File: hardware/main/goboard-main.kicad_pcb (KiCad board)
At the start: 2 copper layers, 304.7 x 114.2 mm, 190 parts, among them J1 USB_C_Receptacle_USB2.0, J2 Conn_02x05_Top_Bottom, J3 Conn_01x01, Q1 SSM3J338R, Q2 BCP53, Q3 SSM3J338R, Q4 BC817, Q5 SSM3J338R, Q6 BC807, Q7 BC817, Q8 BC817, Q9 SSM3J338R, SW1 Esc, SW10 a, SW11 SW_Push, SW12 Fn, SW13 F2, SW14 2, SW15 w, SW16 s, SW17 z, SW18 Tux, SW19 F3, SW2 F1, SW20 3, SW21 e, SW22 d, SW23 c, SW24 Alt, SW25 F4, SW26 4, SW27 r, SW28 f, SW29 v, SW3 tilde, SW30 SW_DP3T, SW31 F5, SW32 5, SW33 t, SW34 g, SW35 b, SW36 F6, SW37 6, SW38 y, SW39 h, SW4 Tab, SW40 n, SW41 F7, SW42 7, SW43 u, SW44 j, SW45 m, SW46 Space, SW47 F8, SW48 8, SW49 i, SW5 Caps Lock, SW50 k, SW51 comma, SW52 F9, SW53 9, SW54 o, SW55 l, SW56 dot, SW57 F10, SW58 0, SW59 p, SW6 Shift, SW60 semicolon, SW61 slash, SW62 Alt Gr, SW63 F11, SW64 minus, SW65 sq br open, SW66 apostrophe, SW67 Menu, SW68 F12, SW69 equal, SW7 Ctrl, SW70 sq br close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

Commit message: Rework the off/bluetooth1/bluetooth2 switch connection
To save energy an external pull-down resistor is added and the off
position is not connected to the MCU.
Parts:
- added R25: 100k, Resistor_SMD:R_0603_1608Metric_Pad0.98x0.95mm_HandSolder, F.Cu at (275.4, 51.5)
- added R26: 100k, Resistor_SMD:R_0603_1608Metric_Pad0.98x0.95mm_HandSolder, F.Cu at (275.4, 49.0)
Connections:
- C1 pad 1: +5V -> GND
- C1 pad 2: GND -> +5V
- C3 pad 1: /VCC_SW -> GND
- C3 pad 2: GND -> /VCC_SW
- SW30 pad 1: /switch_usb_off -> unconnected-(SW30-Pad1)
- U1 pad 3: /switch_bt_2 -> unconnected-(U1-Pad3)
- U1 pad 33: /switch_usb_off -> unconnected-(U1-Pad33)
- U1 pad 35: unconnected-(U1-Pad35) -> /switch_bt_2
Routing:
- net unconnected-(SW30-Pad1): track 0.00 -> 2.50 mm
- net /switch_usb_off: track 2.50 -> 0.00 mm

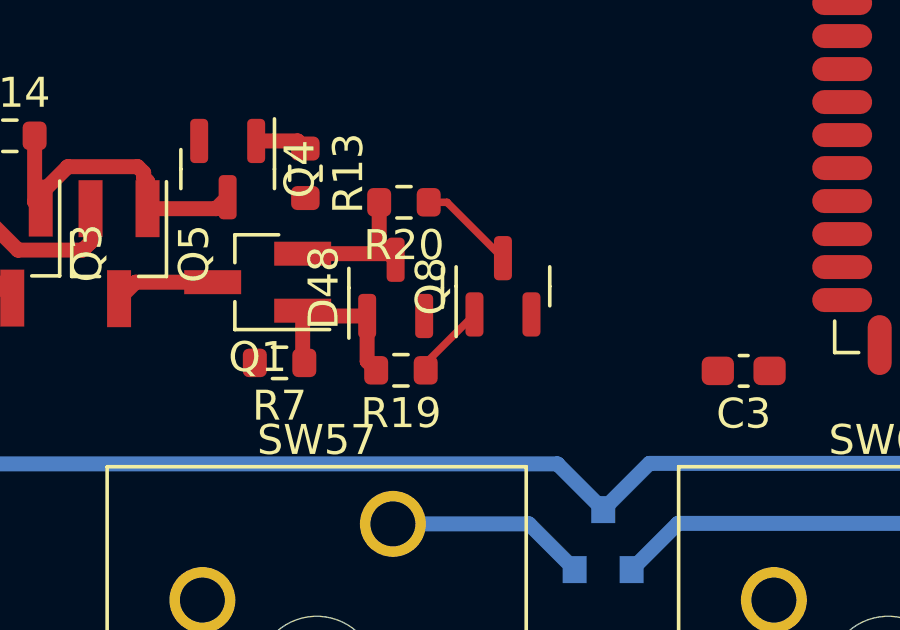
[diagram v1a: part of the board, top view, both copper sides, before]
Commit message: Remove the USB sense curcuit
As V_BUS is connected to the MCU it can detect when the USB is
connected.
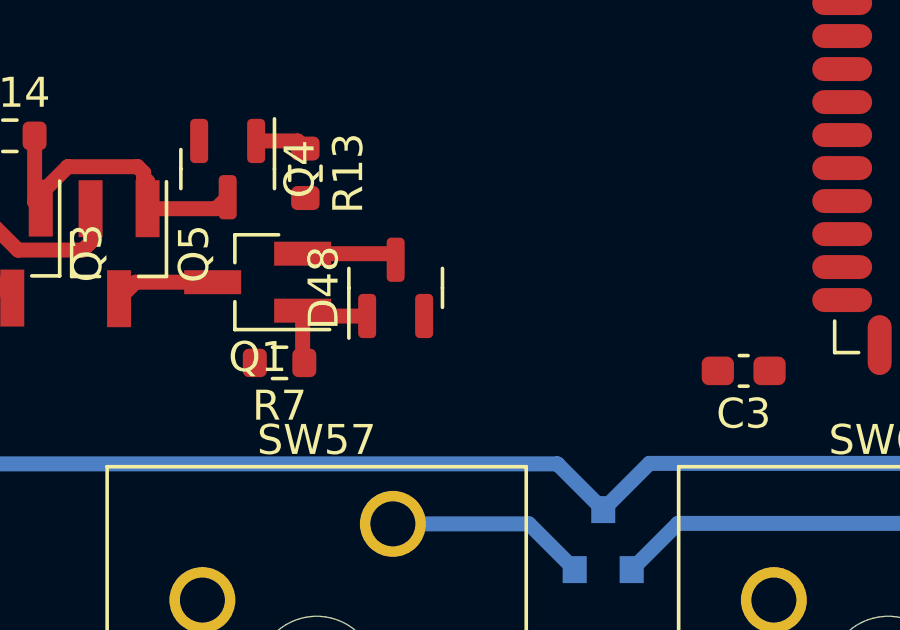
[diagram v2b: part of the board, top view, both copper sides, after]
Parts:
- removed Q8: BC817, Package_TO_SOT_SMD:SOT-23
- removed R19: 4.7K, Resistor_SMD:R_0603_1608Metric
- removed R20: 10K, Resistor_SMD:R_0603_1608Metric
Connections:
- U1 pad 5: /MCU/~USB_CONN -> unconnected-(U1-Pad5)
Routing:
- net /MCU/~USB_CONN: track 3.25 -> 0.00 mm
- net Net-(Q8-Pad1): track 2.54 -> 0.00 mm
- net /VCC_SW: track 21.1 -> 19.0 mm
- net +3V3: track 132.4 -> 130.4 mm

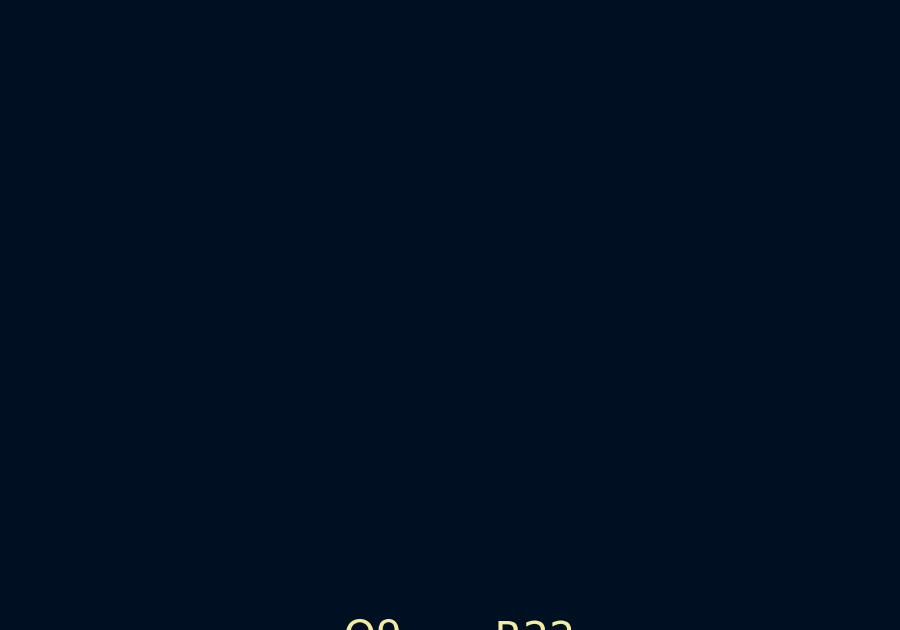
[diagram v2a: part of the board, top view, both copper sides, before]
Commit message: Add circuit to disconnect the shift registers
This is done to save energy when the keyboard is switched off.
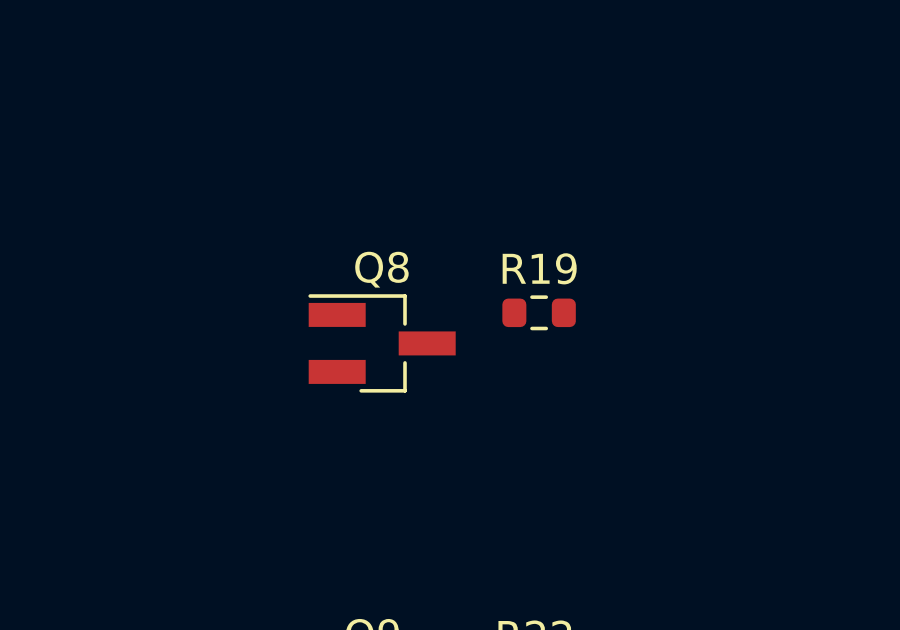
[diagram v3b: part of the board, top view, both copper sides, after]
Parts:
- added Q8: SSM3J338R, Package_TO_SOT_SMD:SOT-23_Handsoldering, F.Cu at (241.8, 41.5)
- added R19: 10K, Resistor_SMD:R_0603_1608Metric, F.Cu at (247.0, 40.5)
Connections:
- C4 pad 1: /VCC_SW -> /VCC_KEYS
- C5 pad 1: /VCC_SW -> /VCC_KEYS
- C6 pad 1: /VCC_SW -> /VCC_KEYS
- U1 pad 3: unconnected-(U1-Pad3) -> /MCU/~ENABLE_VCC_KEYS
- U2 pad 10: /VCC_SW -> /VCC_KEYS
- U2 pad 16: /VCC_SW -> /VCC_KEYS
- U3 pad 16: /VCC_SW -> /VCC_KEYS
- U4 pad 16: /VCC_SW -> /VCC_KEYS
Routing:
- net /VCC_KEYS: track 0.00 -> 13.3 mm, vias 0 -> 2
- net /VCC_SW: track 19.0 -> 5.68 mm, vias 2 -> 0

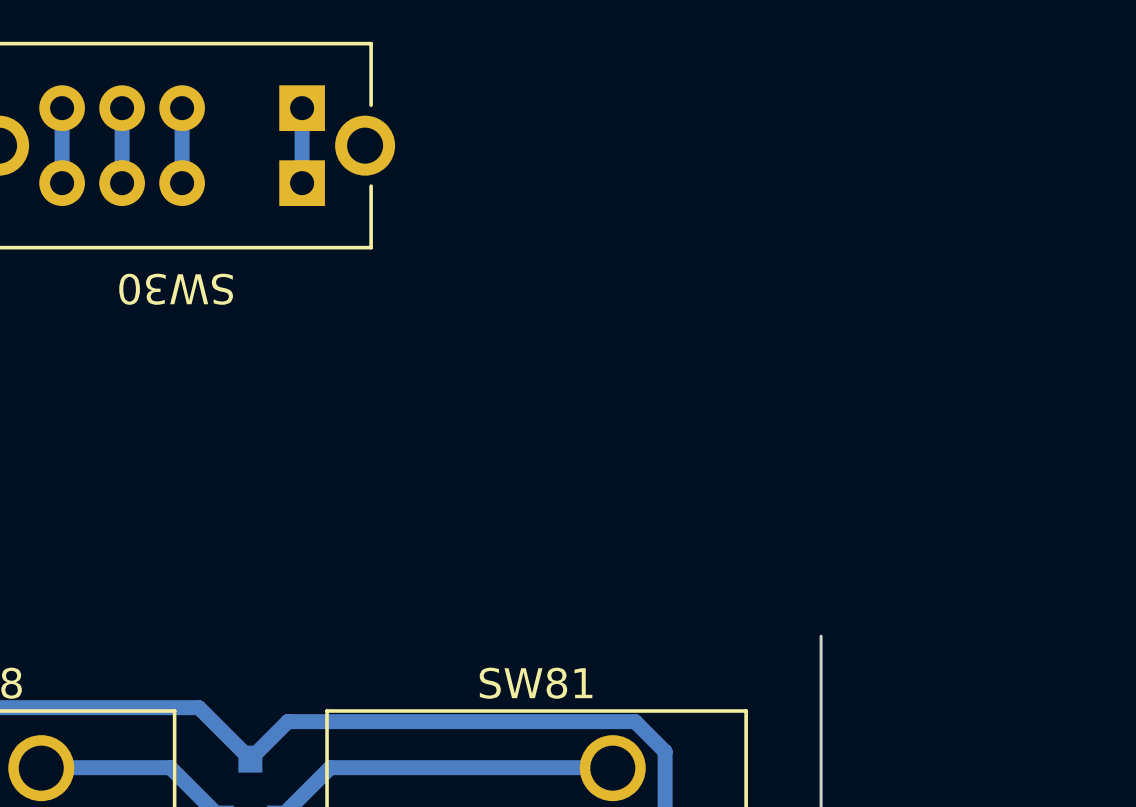
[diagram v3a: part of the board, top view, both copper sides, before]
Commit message: Rework the connection to the numpad
Changes:
- The UART lines now have a protection circuit
- The power supply line of the numpad can be switched on and off by the MCU.
- An Id-line is added so that the MCU can detect when the numpad is
  connected.
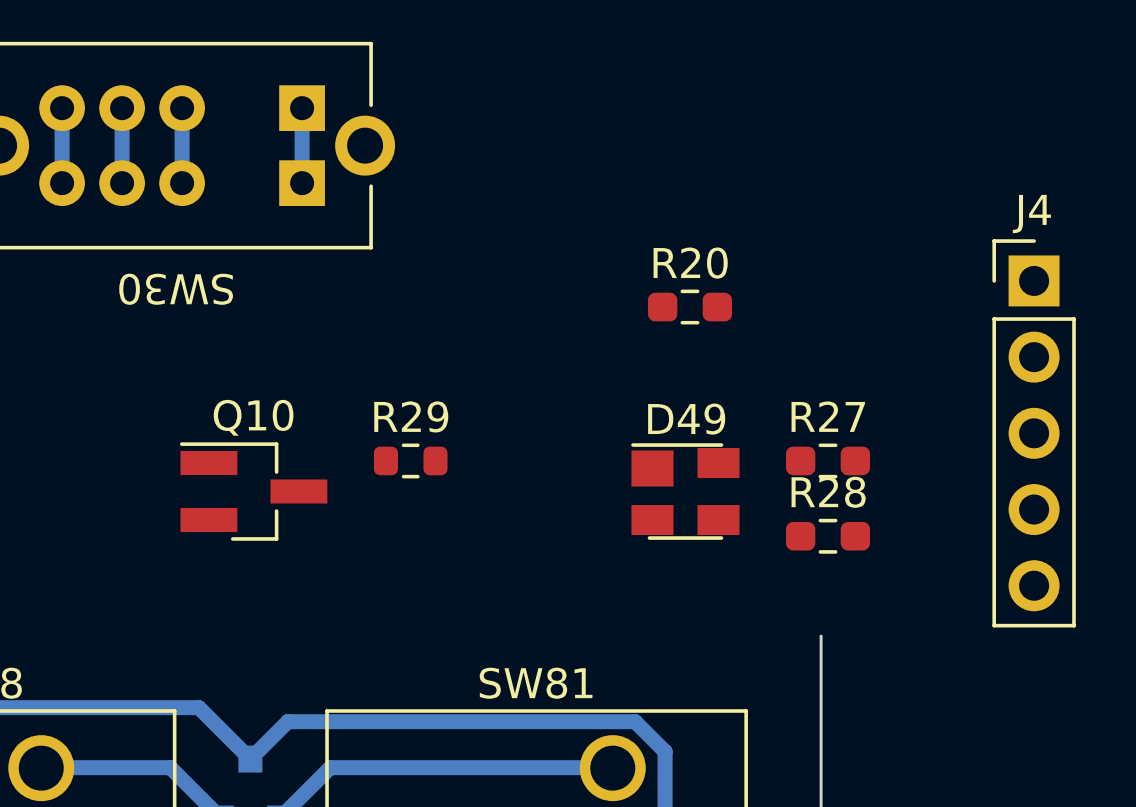
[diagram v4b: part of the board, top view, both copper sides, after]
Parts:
- added D49: PRTR5V0U2X, Package_TO_SOT_SMD:SOT-143, F.Cu at (338.2, 67.0)
- added J4: Conn_01x05, Connector_PinHeader_2.54mm:PinHeader_1x05_P2.54mm_Vertical, F.Cu at (349.8, 60.0)
- added Q10: SSM3J338R, Package_TO_SOT_SMD:SOT-23_Handsoldering, F.Cu at (323.8, 67.0)
- added R20: 1M, Resistor_SMD:R_0603_1608Metric_Pad0.98x0.95mm_HandSolder, F.Cu at (338.3, 60.8)
- added R27: 100, Resistor_SMD:R_0603_1608Metric_Pad0.98x0.95mm_HandSolder, F.Cu at (342.9, 66.0)
- added R28: 100, Resistor_SMD:R_0603_1608Metric_Pad0.98x0.95mm_HandSolder, F.Cu at (342.9, 68.5)
- added R29: 10K, Resistor_SMD:R_0603_1608Metric, F.Cu at (329.0, 66.0)
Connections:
- U1 pad 33: unconnected-(U1-Pad33) -> /~NUMPAD_ID
- U1 pad 36: unconnected-(U1-Pad36) -> /MCU/~ENABLE_VCC_NUMPAD

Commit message: WIP: Design of PCB
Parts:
- D49, R20: moved to B.Cu
- moved R28 71.0 mm to (272.0, 71.5), turned to 180 degrees
- moved R27 67.5 mm to (275.6, 71.5)
- moved Q8 51.8 mm to (285.7, 69.1)
- moved R25 47.2 mm to (321.6, 61.3), turned to 90 degrees
- moved R19 46.6 mm to (285.6, 66.5), turned to 180 degrees
- moved R26 43.8 mm to (317.4, 61.3), turned to -90 degrees
- moved J4 43.5 mm to (324.6, 95.3)
- moved R20 42.1 mm to (321.8, 99.5), turned to -90 degrees
- moved D49 41.1 mm to (320.9, 104.2), turned to -90 degrees
- moved R29 34.7 mm to (294.3, 66.5), turned to 180 degrees
- moved Q10 29.3 mm to (294.5, 69.0)
- moved R23 23.5 mm to (226.1, 71.7), turned to -90 degrees
- moved R22 23.3 mm to (233.2, 71.7), turned to -90 degrees
- moved Q9 21.5 mm to (229.7, 71.7), turned to 180 degrees
- moved R24 21.4 mm to (224.6, 71.7), turned to 90 degrees
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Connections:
- D49 pad 2: /UART_TX -> Net-(D49-Pad2)
- D49 pad 3: /UART_RX -> Net-(D49-Pad3)
- J4 pad 4: Net-(J4-Pad4) -> Net-(D49-Pad2)
- J4 pad 5: Net-(J4-Pad5) -> Net-(D49-Pad3)
- R27 pad 2: Net-(J4-Pad4) -> Net-(D49-Pad2)
- R28 pad 2: Net-(J4-Pad5) -> Net-(D49-Pad3)
- U1 pad 10: /MCU/MEAS_V_BATT -> /MCU/~ACT_MEAS_V_BATT
- U1 pad 11: /MCU/~ACT_MEAS_V_BATT -> /MCU/MEAS_V_BATT
- U1 pad 12: /UART_RX -> /MCU/SPI_MOSI
- U1 pad 16: /MCU/SPI_MOSI -> unconnected-(U1-Pad16)
- U1 pad 19: unconnected-(U1-Pad19) -> /UART_RX
- U1 pad 26: unconnected-(U1-Pad26) -> /MCU/~ENABLE_VCC_KEYS
- U1 pad 3: /MCU/~ENABLE_VCC_KEYS -> unconnected-(U1-Pad3)
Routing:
- net /MCU/V_MID: track 1.60 -> 66.0 mm, vias 0 -> 2
- net /MCU/~BAL_HIGH: track 0.00 -> 62.2 mm, vias 0 -> 2
- net /MCU/BAL_LOW: track 0.00 -> 55.3 mm
- net /MCU/MEAS_V_BATT: track 0.00 -> 34.2 mm
- net /MCU/~ENABLE_VCC_NUMPAD: track 0.00 -> 28.8 mm
- net /MCU/~ACT_MEAS_V_BATT: track 0.00 -> 27.3 mm
- net /MCU/CHARGE: track 0.00 -> 18.8 mm
- net /MCU/~ENABLE_VCC_KEYS: track 0.00 -> 15.4 mm
- net /VCC_SW: track 5.68 -> 18.3 mm
- net +BATT: track 237.1 -> 241.2 mm
- net /switch_bt_1: track 2.50 -> 6.25 mm
- net /switch_bt_2: track 2.50 -> 6.19 mm
- net Net-(D49-Pad2): track 0.00 -> 2.75 mm
- net /~NUMPAD_ID: track 0.00 -> 2.75 mm
- net Net-(D49-Pad3): track 0.00 -> 2.75 mm
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
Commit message: WIP: Design of PCB
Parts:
- moved D47 43.1 mm to (304.0, 68.0), turned to -90 degrees
- moved R6 40.8 mm to (306.2, 64.2)
- moved D46 37.2 mm to (314.0, 68.0), turned to -90 degrees
- moved D45 33.6 mm to (324.0, 68.0), turned to -90 degrees
- moved R5 33.1 mm to (314.0, 63.0), turned to 90 degrees
- moved R4 27.9 mm to (324.0, 63.0), turned to 90 degrees
- moved R28 3.75 mm to (275.7, 72.2), turned to 0 degrees
- moved R27 2.26 mm to (275.7, 73.8)
- moved R19 1.29 mm to (284.3, 66.5)
- moved C1 1.00 mm to (265.9, 73.6)
- moved Q8 0.32 mm to (285.4, 69.1)
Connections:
- D46 pad 2: Net-(D46-Pad2) -> Net-(U1-Pad29)
- D47 pad 2: Net-(D47-Pad2) -> Net-(U1-Pad30)
- U1 pad 12: /MCU/SPI_MOSI -> /MCU/SPI_MISO
- U1 pad 13: /MCU/SPI_MISO -> /MCU/SPI_MOSI
- U1 pad 15: /MCU/165_~CE -> /MCU/165_~PL
- U1 pad 17: /MCU/165_~PL -> /MCU/165_~CE
- U1 pad 29: Net-(D47-Pad2) -> Net-(U1-Pad29)
- U1 pad 30: Net-(D46-Pad2) -> Net-(U1-Pad30)
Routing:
- net /MCU/SPI_SCK: track 0.65 -> 288.4 mm, vias 0 -> 16
- net /MCU/165_~PL: track 0.00 -> 189.3 mm, vias 0 -> 5
- net /MCU/165_~CE: track 0.00 -> 168.8 mm, vias 0 -> 3
- net Net-(U3-Pad10): track 0.00 -> 165.4 mm, vias 0 -> 2
- net /VCC_KEYS: track 13.3 -> 177.9 mm
- net /MCU/SPI_MISO: track 0.00 -> 164.3 mm, vias 0 -> 5
- net /MCU/SPI_MOSI: track 0.00 -> 122.4 mm, vias 0 -> 9
- net Net-(SW78-Pad2): track 68.0 -> 167.5 mm, vias 4 -> 11
- net /SWDIO: track 91.5 -> 173.6 mm, vias 7 -> 11
- net /switch_bt_1: track 6.25 -> 72.8 mm, vias 0 -> 2
- net /switch_bt_2: track 6.19 -> 65.2 mm, vias 0 -> 2
- net Net-(D45-Pad2): track 0.00 -> 58.0 mm, vias 0 -> 2
- net Net-(U1-Pad29): track 0.00 -> 47.7 mm, vias 0 -> 2
- net /USB_D-: track 5.36 -> 51.7 mm, vias 0 -> 2
- net /USB_D+: track 5.11 -> 46.8 mm, vias 0 -> 2
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
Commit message: WIP: Design of PCB
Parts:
- moved R20 37.0 mm to (328.2, 63.0)
- moved D49 37.0 mm to (327.3, 67.8)
- moved J4 37.0 mm to (330.9, 58.9)
- moved D45 3.41 mm to (320.6, 67.6), turned to 180 degrees
- moved R4 3.16 mm to (321.5, 65.0)
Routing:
- net /VCC_KEYS: track 177.9 -> 334.9 mm, vias 2 -> 17
- net Net-(SW81-Pad2): track 100.4 -> 169.7 mm, vias 7 -> 11
- net /~NUMPAD_ID: track 2.75 -> 66.9 mm, vias 0 -> 3
- net /VCC_SW: track 36.8 -> 100.2 mm, vias 0 -> 6
- net Net-(D49-Pad2): track 2.75 -> 64.2 mm
- net Net-(D49-Pad3): track 2.75 -> 56.9 mm, vias 0 -> 1
- net /VCC_SW_NUMPAD: track 0.00 -> 41.4 mm, vias 0 -> 4
- net /MCU/165_~CE: track 168.8 -> 205.3 mm, vias 3 -> 7
- net GND: track 53.3 -> 76.3 mm, vias 2 -> 5
- net Net-(D45-Pad2): track 58.0 -> 54.2 mm
- net /MCU/SPI_SCK: track 288.4 -> 291.8 mm, vias 16 -> 18
- net /MCU/~ENABLE_VCC_NUMPAD: track 28.8 -> 30.6 mm
- net Net-(D45-Pad1): track 3.21 -> 1.76 mm
- net Net-(SW74-Pad2): track 160.4 -> 161.1 mm
